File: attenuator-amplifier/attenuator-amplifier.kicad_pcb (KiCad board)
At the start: 4 copper layers, 61 parts, among them J1 IN, J2 AOUT, J3 V_{REF}, J4 COM, J5 PWR, K1 G6KU-2, K2 G6KU-2, K3 G6KU-2, U1 DG4052E, U2 OPA197xDBV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

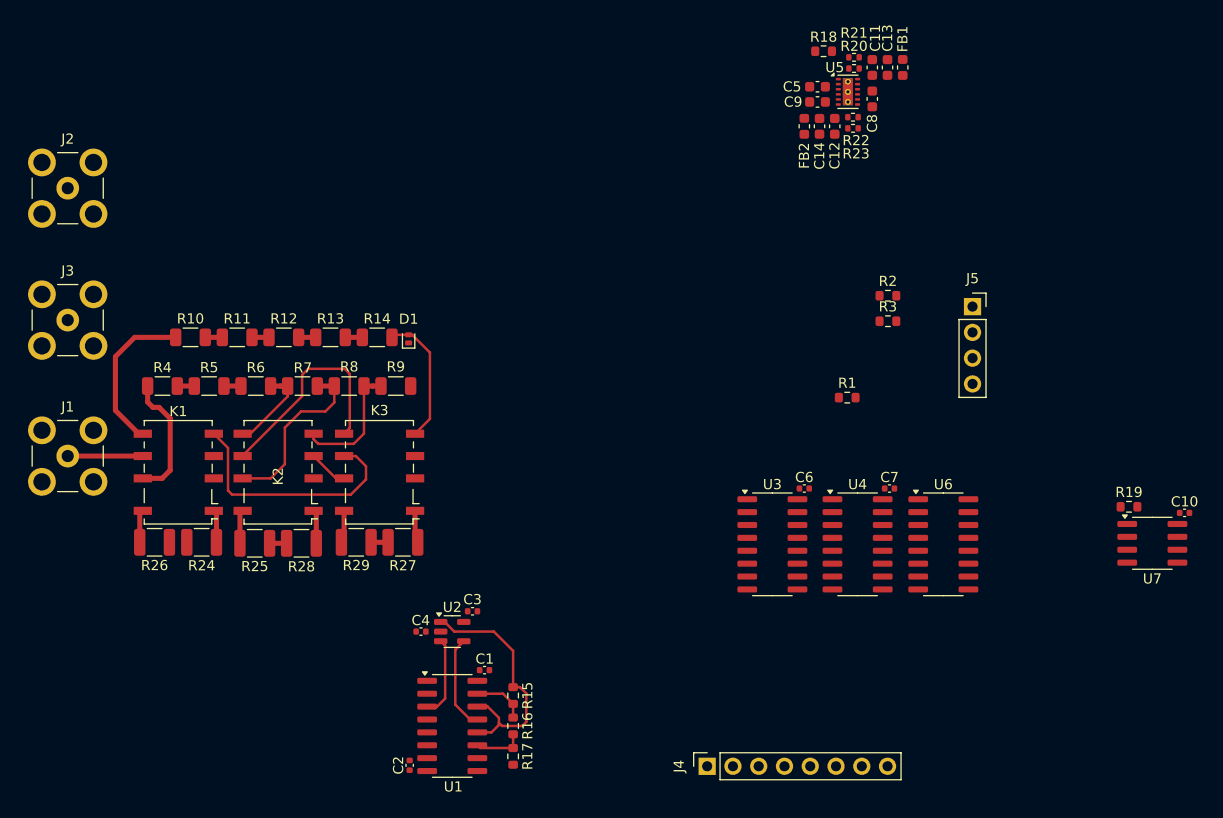
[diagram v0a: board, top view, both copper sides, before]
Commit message: small changes, add missing part numbers
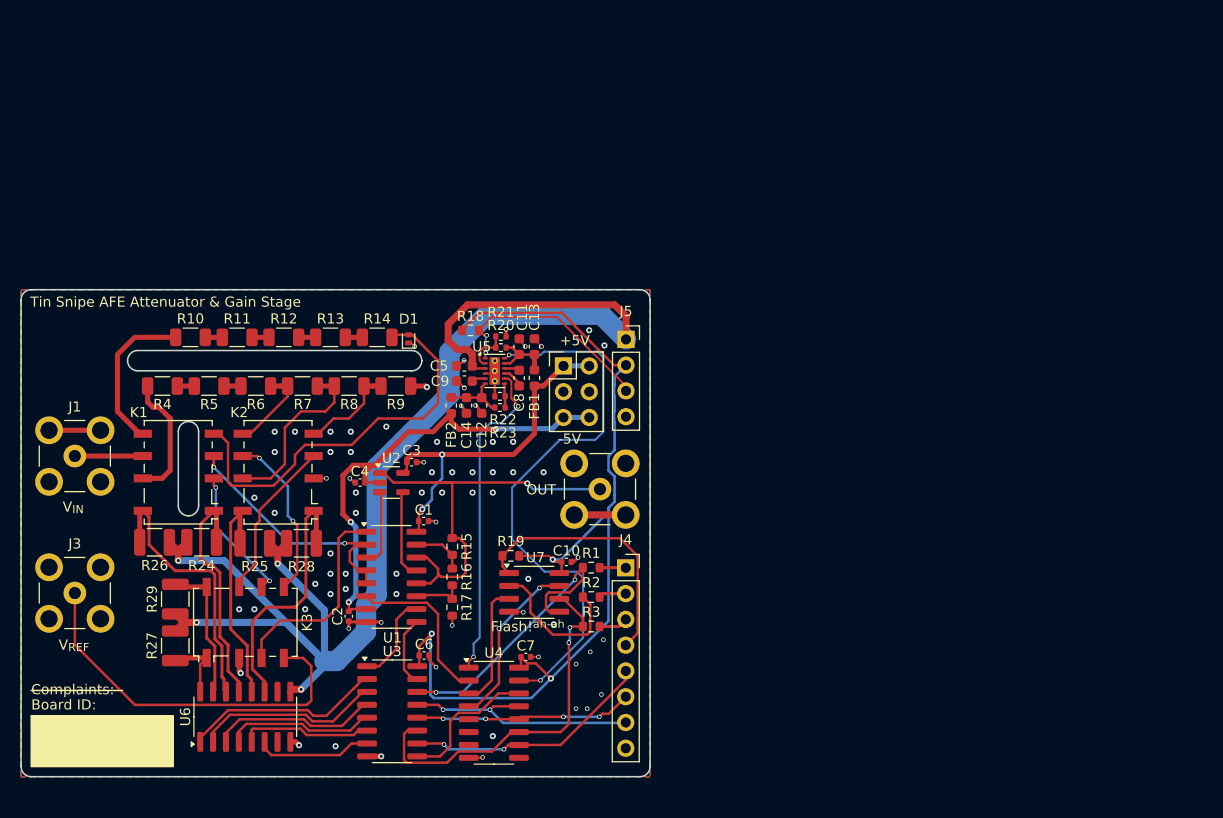
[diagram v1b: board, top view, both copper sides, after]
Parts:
- added J6: Bias Power, Connector_PinHeader_2.54mm:PinHeader_2x03_P2.54mm_Vertical, F.Cu at (127.0, 81.5)
- C1, C10, C2, C3, C4, C6, C7: value 100nF -> 100n
- moved U6 70.9 mm to (95.6, 116.1), turned to 90 degrees
- moved C10 61.1 mm to (127.3, 100.8)
- moved U7 61.1 mm to (124.1, 103.8)
- moved R19 61.1 mm to (121.8, 100.2)
- moved J2 60.3 mm to (130.6, 93.7)
- moved FB1 47.5 mm to (124.1, 82.7), turned to -90 degrees
- moved C8 44.4 mm to (122.6, 82.7)
- moved C11 44.4 mm to (122.6, 79.6)
- moved C13 44.4 mm to (124.1, 79.6)
- moved C5 44.4 mm to (117.2, 81.5)
- moved C9 44.4 mm to (117.2, 83.0)
- moved R18 44.4 mm to (117.8, 78.0)
- moved R20 44.4 mm to (120.8, 79.7)
- moved R22 44.4 mm to (120.7, 84.5)
- moved U5 44.4 mm to (120.2, 82.0)
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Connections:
- J2 pad 1: /ADC_{IN} -> /G1
- K1 pad 2: /G1 -> /ATT_{OUT}
- K1 pad 3: /ADC_{IN} -> /GS_{IN}
- K1 pad 4: /ATT_{OUT} -> /V_{LOW}
- K3 pad 3: /GS_{IN} -> /V_{CAL}
- K3 pad 4: /V_{LOW} -> /V_{REF}
- R24 pad 1: +5V -> +5V2
- R25 pad 1: +5V -> +5V2
- R26 pad 1: +5V -> +5V2
- R27 pad 1: +5V -> +5V2
- R28 pad 1: +5V -> +5V2
- R29 pad 1: +5V -> +5V2
- U1 pad 1: /V_{REF} -> /V_{CAL}
- U3 pad 1: Net-(U3-QB) -> /GS_{A}
- U3 pad 15: Net-(U3-QA) -> /GS_{B}
- U3 pad 6: /GS_{A} -> Net-(U3-QG)
- U3 pad 7: /GS_{B} -> Net-(U3-QH)
- U6 pad 1: Net-(U3-QA) -> Net-(U3-QC)
- U6 pad 11: /R3_{+R} -> /R2_{+S}
- U6 pad 12: /R3_{+S} -> /R2_{+R}
- U6 pad 13: /R2_{+R} -> /R1_{+S}
- U6 pad 14: /R2_{+S} -> /R1_{+R}
- U6 pad 15: /R1_{+R} -> /R3_{+R}
- U6 pad 16: /R1_{+S} -> /R3_{+S}
- U6 pad 2: Net-(U3-QB) -> Net-(U3-QD)
- U6 pad 3: Net-(U3-QC) -> Net-(U3-QE)
- U6 pad 4: Net-(U3-QD) -> Net-(U3-QF)
- U6 pad 5: Net-(U3-QE) -> Net-(U3-QG)
- U6 pad 6: Net-(U3-QF) -> Net-(U3-QH)
- U6 pad 9: +5V -> +5V2
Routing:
- net +5V2: track 0.00 -> 143.9 mm, vias 0 -> 4
- net +3V3: track 0.00 -> 94.7 mm, vias 0 -> 3
- net /BS_{EN+}: track 0.00 -> 56.5 mm, vias 0 -> 2
- net -5V: track 0.00 -> 52.8 mm, vias 0 -> 3
- net GND: track 0.00 -> 40.1 mm, vias 0 -> 72
- net /V_{REF}: track 0.00 -> 37.5 mm
- net /SCLK: track 0.00 -> 36.7 mm, vias 0 -> 2
- net /BS_{EN-}: track 0.00 -> 31.9 mm, vias 0 -> 2
- net +5V: track 3.35 -> 34.7 mm, vias 0 -> 2
- net /COPI: track 0.00 -> 29.8 mm, vias 0 -> 2
- net /V_{LOW}: track 13.2 -> 40.3 mm
- net /EEP_{~{CS}}: track 0.00 -> 26.0 mm
- net /GS_{IN}: track 0.00 -> 25.5 mm, vias 0 -> 2
- net /R_{~{SRCLR}}: track 0.00 -> 24.5 mm, vias 0 -> 2
- net /R_{~{OE}}: track 0.00 -> 24.3 mm, vias 0 -> 2
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- added copper zone on B.Cu, net GND
- added copper zone on F.Cu, net GND
- added copper zone on In1.Cu, net GND
- added copper zone on In2.Cu, net GND
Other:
- board outline added: 62 x 48 mm
- board text added: "+5V"
- board text added: "-5V"
- board text added: "Board ID:"
- board text added: "Complaints:"
- board text added: "Flash!^{ah-ah}"
- board text added: "OUT"
- board text added: "OpAmp:"
- board text added: "Relay:"
- board text added: "This will be a realy quick one, I thought and then did a deep dive into the intricacies of how to save a few cents on the relay driving circuits and almost descendet into madness. - ln {dblquote}I'm innocent in this{dblquote} - Nina, totally innocent"
- board text added: "Tin Snipe AFE Attenuator & Gain Stage"
- board text added: "V_{IN}"
- board text added: "V_{REF}"
